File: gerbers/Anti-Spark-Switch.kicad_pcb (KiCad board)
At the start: 2 copper layers, 63.2 x 42 mm, 18 parts, among them P1 Pad_Conn, P2 Pad_Conn, P3 Screw_Terminal, P4 Screw_Terminal, P5 Pad_Conn, P6 Pad_Conn, P7 CONN_01X04, Q1 IRFS7530, Q2 IRFS7530, Q3 IRFS7530

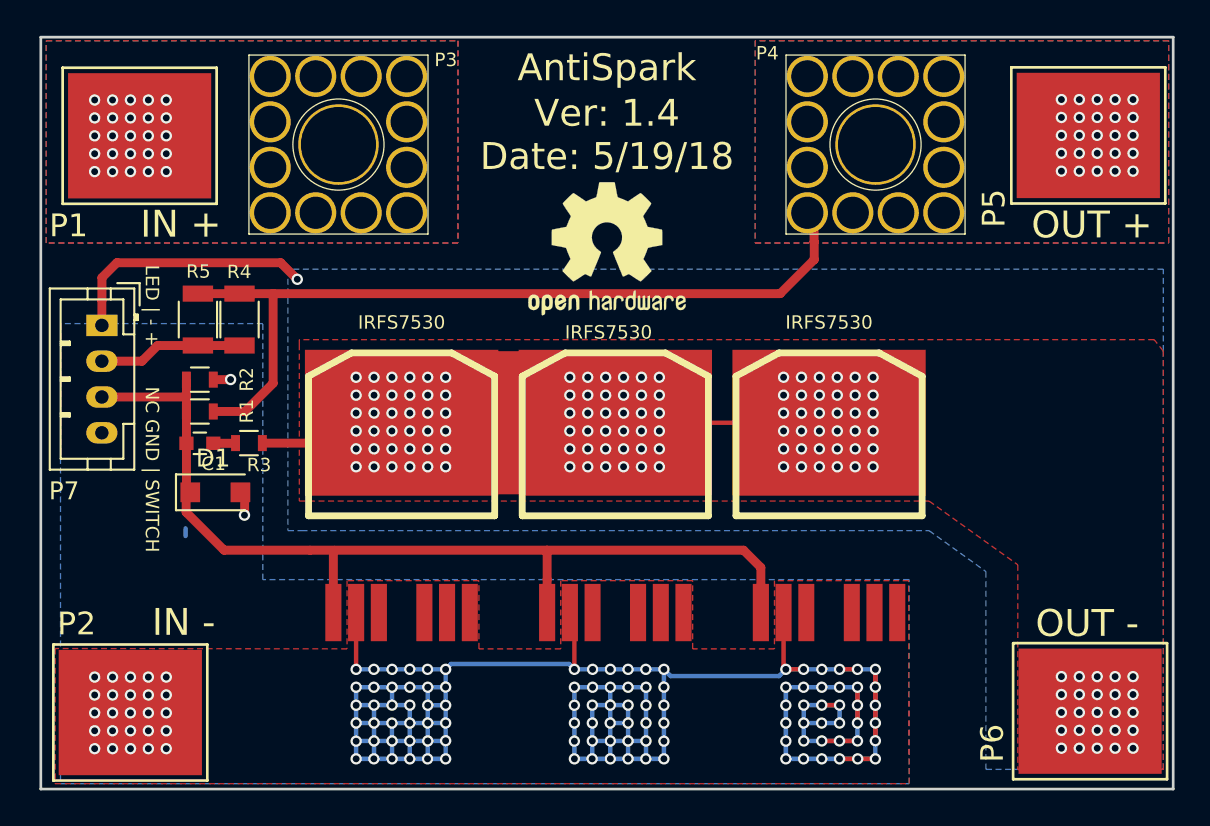
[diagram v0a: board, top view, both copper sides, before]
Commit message: Generated new gerbers for no fuse and fixed file names
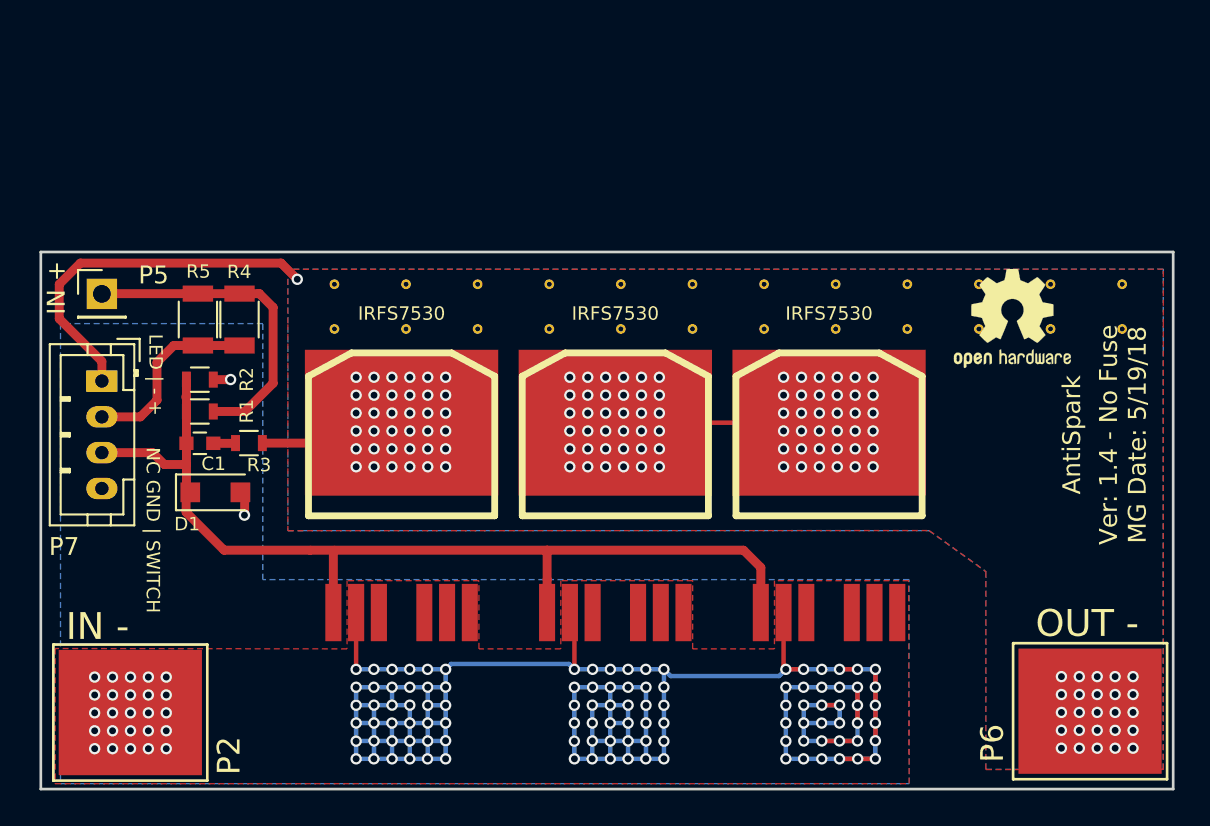
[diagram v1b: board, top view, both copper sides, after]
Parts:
- removed P1: Pad_Conn, sparkparts:1PAD_8x7mm
- removed P3, P4: Screw_Terminal, sparkparts:M5_Screw_Terminal_12_pin
- removed the REF*** at (147.3, 88.6)
- added ?: , Kinetic_Footprints:via-0.45mm, F.Cu at (176.1, 93.1)
- added ?: , Kinetic_Footprints:via-0.45mm, F.Cu at (140.1, 93.1)
- added ?: , Kinetic_Footprints:via-0.45mm, F.Cu at (136.1, 93.1)
- added ?: , Kinetic_Footprints:via-0.45mm, F.Cu at (132.1, 93.1)
- added ?: , Kinetic_Footprints:via-0.45mm, F.Cu at (176.1, 90.6)
- added ?: , Kinetic_Footprints:via-0.45mm, F.Cu at (172.1, 90.6)
- added ?: , Kinetic_Footprints:via-0.45mm, F.Cu at (168.1, 90.6)
- added ?: , Kinetic_Footprints:via-0.45mm, F.Cu at (164.1, 90.6)
- added ?: , Kinetic_Footprints:via-0.45mm, F.Cu at (160.1, 90.6)
- added ?: , Kinetic_Footprints:via-0.45mm, F.Cu at (156.1, 90.6)
- added ?: , Kinetic_Footprints:via-0.45mm, F.Cu at (152.1, 90.6)
- added ?: , Kinetic_Footprints:via-0.45mm, F.Cu at (172.1, 93.1)
- added ?: , Kinetic_Footprints:via-0.45mm, F.Cu at (148.1, 90.6)
- added ?: , Kinetic_Footprints:via-0.45mm, F.Cu at (144.1, 90.6)
- added ?: , Kinetic_Footprints:via-0.45mm, F.Cu at (140.1, 90.6)
- added ?: , Kinetic_Footprints:via-0.45mm, F.Cu at (136.1, 90.6)
- added ?: , Kinetic_Footprints:via-0.45mm, F.Cu at (132.1, 90.6)
- added ?: , Kinetic_Footprints:via-0.45mm, F.Cu at (168.1, 93.1)
- added ?: , Kinetic_Footprints:via-0.45mm, F.Cu at (164.1, 93.1)
- added ?: , Kinetic_Footprints:via-0.45mm, F.Cu at (160.1, 93.1)
- added ?: , Kinetic_Footprints:via-0.45mm, F.Cu at (156.1, 93.1)
- added ?: , Kinetic_Footprints:via-0.45mm, F.Cu at (152.1, 93.1)
- added ?: , Kinetic_Footprints:via-0.45mm, F.Cu at (148.1, 93.1)
- added ?: , Kinetic_Footprints:via-0.45mm, F.Cu at (144.1, 93.1)
- added G***: LOGO, w_logo:Logo_silk_high_voltage_10x8.5mm, B.Cu at (147.8, 106.3)
- added REF***: OSHW-Logo2_7.3x6mm_SilkScreen, Symbols:OSHW-Logo2_7.3x6mm_SilkScreen, F.Cu at (170.0, 92.5)
- P5: footprint sparkparts:1PAD_8x7mm -> Connector_PinHeader_2.54mm:PinHeader_1x01_P2.54mm_Vertical
- moved P5 55.8 mm to (119.1, 91.1)
- moved P7 3.11 mm to (119.1, 96.0)
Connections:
- P5 pad 1: Net-(P4-Pad1) -> VCC
- R1 pad 1: Net-(P4-Pad1) -> VCC
- R4 pad 1: Net-(P4-Pad1) -> VCC
- R5 pad 1: Net-(P4-Pad1) -> VCC
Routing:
- net Net-(P4-Pad1): track 73.7 -> 0.00 mm, vias 25 -> 0
- net VCC: track 26.8 -> 18.1 mm, vias 25 -> 0
- net Net-(P6-Pad1): track 121.9 -> 116.3 mm
- net Net-(P7-Pad2): track 8.05 -> 10.6 mm
- removed copper zone on B.Cu, net Net-(P4-Pad1)
- removed copper zone on F.Cu, net Net-(P4-Pad1)
- removed copper zone on B.Cu, net VCC
- removed copper zone on F.Cu, net VCC
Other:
- board size 63.2 x 42 mm -> 63.2 x 30 mm
- net class Default: clearance 0.13 -> 0
- rule trace_clearance: 0.13 -> 0
- board text added: "Ver: 1.4 - No Fuse MG Date: 5/19/18"
- board text removed: "OUT +"
- board text removed: "Ver: 1.4 Date: 5/19/18"
